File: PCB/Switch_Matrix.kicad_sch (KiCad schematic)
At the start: 28 parts, among them SW3 RotaryEncoder_Switch, SW4 RotaryEncoder_Switch

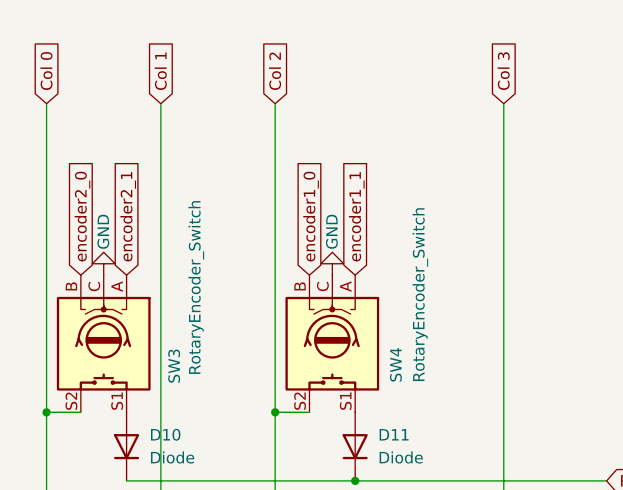
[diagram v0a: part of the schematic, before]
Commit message: Schema for V2 Did some cleanup and seperated the switch matrix to it's own file fixes #1
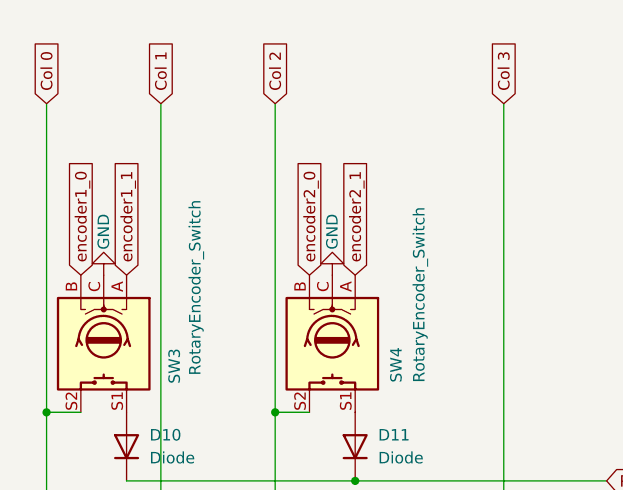
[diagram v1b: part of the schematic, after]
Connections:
- net encoder1_0: now also SW3.B; no longer SW4.B
- net encoder1_1: now also SW3.A; no longer SW4.A
- net encoder2_0: now also SW4.B; no longer SW3.B
- net encoder2_1: now also SW4.A; no longer SW3.A
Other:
- company: (none) -> KillrOfLife
- title: (none) -> Macro32
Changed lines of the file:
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@@
 	(generator_version "9.0")
 	(paper "A4")
+	(title_block
+		(title "Macro32")
+		(date "2025-11-08")
+		(rev "v2")
+		(company "KillrOfLife")
+	)
 	(junction
 		(at 72.39 128.27)
@@
 		)
 	)
+	(global_label "Col 1"
+		(shape input)
+		(at 54.61 38.1 90)
+		(fields_autoplaced yes)
+		(effects
+			(font
+				(size 1.27 1.27)
+			)
+			(justify left)
+		)
+		(property "Intersheetrefs" "${INTERSHEET_REFS}"
+			(at 54.61 29.8535 90)
+			(effects
+				(font
+					(size 1.27 1.27)
+				)
+				(justify left)
+				(hide yes)
+			)
+		)
+	)
+	(global_label "Col 0"
+		(shape input)
+		(at 41.91 38.1 90)
+		(fields_autoplaced yes)
+		(effects
+			(font
+				(size 1.27 1.27)
+			)
+			(justify left)
+		)
+		(property "Intersheetrefs" "${INTERSHEET_REFS}"
+			(at 41.91 29.8535 90)
+			(effects
+				(font
+					(size 1.27 1.27)
+				)
+				(justify left)
+				(hide yes)
+			)
+		)
+	)
+	(global_label "Col 2"
+		(shape input)
+		(at 67.31 38.1 90)
+		(fields_autoplaced yes)
+		(effects
+			(font
+				(size 1.27 1.27)
+			)
+			(justify left)
+		)
+		(property "Intersheetrefs" "${INTERSHEET_REFS}"
+			(at 67.31 29.8535 90)
+			(effects
+				(font
+					(size 1.27 1.27)
+				)
+				(justify left)
+				(hide yes)
+			)
+		)
+	)
+	(global_label "Row 0"
+		(shape input)
+		(at 104.14 80.01 0)
+		(fields_autoplaced yes)
+		(effects
+			(font
+				(size 1.27 1.27)
+			)
+			(justify left)
+		)
+		(property "Intersheetrefs" "${INTERSHEET_REFS}"
+			(at 113.0518 80.01 0)
+			(effects
+				(font
+					(size 1.27 1.27)
+				)
+				(justify left)
+				(hide yes)
+			)
+		)
+	)
+	(global_label "encoder1_1"
+		(shape input)
+		(at 50.8 57.15 90)
+		(fields_autoplaced yes)
+		(effects
+			(font
+				(size 1.27 1.27)
+			)
+			(justify left)
+		)
+		(property "Intersheetrefs" "${INTERSHEET_REFS}"
+			(at 50.8 43.2792 90)
+			(effects
+				(font
+					(size 1.27 1.27)
+				)
+				(justify left)
+				(hide yes)
+			)
+		)
+	)
+	(global_label "Row 3"
+		(shape input)
+		(at 105.41 153.67 0)
+		(fields_autoplaced yes)
+		(effects
+			(font
+				(size 1.27 1.27)
+			)
+			(justify left)
+		)
+		(property "Intersheetrefs" "${INTERSHEET_REFS}"
+			(at 114.3218 153.67 0)
+			(effects
+				(font
+					(size 1.27 1.27)
+				)
+				(justify left)
+				(hide yes)
+			)
+		)
+	)
+	(global_label "encoder2_1"
+		(shape input)
+		(at 76.2 57.15 90)
+		(fields_autoplaced yes)
+		(effects
+			(font
+				(size 1.27 1.27)
+			)
+			(justify left)
+		)
+		(property "Intersheetrefs" "${INTERSHEET_REFS}"
+			(at 76.2 43.2792 90)
+			(effects
+				(font
+					(size 1.27 1.27)
+				)
+				(justify left)
+				(hide yes)
+			)
+		)
+	)
 	(global_label "encoder2_0"
 		(shape input)
+		(at 71.12 57.15 90)
+		(fields_autoplaced yes)
+		(effects
+			(font
+				(size 1.27 1.27)
+			)
+			(justify left)
+		)
+		(property "Intersheetrefs" "${INTERSHEET_REFS}"
+			(at 71.12 43.2792 90)
+			(effects
+				(font
+					(size 1.27 1.27)
+				)
+				(justify left)
+				(hide yes)
+			)
+		)
+	)
+	(global_label "encoder1_0"
+		(shape input)
 		(at 45.72 57.15 90)
 		(fields_autoplaced yes)
@@
 			(effects
 				(font
-					(size 1.27 1.27)
-				)
-				(justify left)
-				(hide yes)
-			)
-		)
-	)
-	(global_label "encoder1_1"
-		(shape input)
-		(at 76.2 57.15 90)
-		(fields_autoplaced yes)
-		(effects
-			(font
-				(size 1.27 1.27)
-			)
-			(justify left)
-		)
-		(property "Intersheetrefs" "${INTERSHEET_REFS}"
-			(at 76.2 43.2792 90)
-			(effects
-				(font
-					(size 1.27 1.27)
-				)
-				(justify left)
-				(hide yes)
-			)
-		)
-	)
-	(global_label "Col 1"
-		(shape input)
-		(at 54.61 38.1 90)
-		(fields_autoplaced yes)
-		(effects
-			(font
-				(size 1.27 1.27)
-			)
-			(justify left)
-		)
-		(property "Intersheetrefs" "${INTERSHEET_REFS}"
-			(at 54.61 29.8535 90)
-			(effects
-				(font
-					(size 1.27 1.27)
-				)
-				(justify left)
-				(hide yes)
-			)
-		)
-	)
-	(global_label "Col 0"
-		(shape input)
-		(at 41.91 38.1 90)
-		(fields_autoplaced yes)
-		(effects
-			(font
-				(size 1.27 1.27)
-			)
-			(justify left)
-		)
-		(property "Intersheetrefs" "${INTERSHEET_REFS}"
-			(at 41.91 29.8535 90)
-			(effects
-				(font
-					(size 1.27 1.27)
-				)
-				(justify left)
-				(hide yes)
-			)
-		)
-	)
-	(global_label "Col 2"
-		(shape input)
-		(at 67.31 38.1 90)
-		(fields_autoplaced yes)
-		(effects
-			(font
-				(size 1.27 1.27)
-			)
-			(justify left)
-		)
-		(property "Intersheetrefs" "${INTERSHEET_REFS}"
-			(at 67.31 29.8535 90)
-			(effects
-				(font
-					(size 1.27 1.27)
-				)
-				(justify left)
-				(hide yes)
-			)
-		)
-	)
-	(global_label "encoder2_1"
-		(shape input)
-		(at 50.8 57.15 90)
-		(fields_autoplaced yes)
-		(effects
-			(font
-				(size 1.27 1.27)
-			)
-			(justify left)
-		)
-		(property "Intersheetrefs" "${INTERSHEET_REFS}"
-			(at 50.8 43.2792 90)
-			(effects
-				(font
-					(size 1.27 1.27)
-				)
-				(justify left)
-				(hide yes)
-			)
-		)
-	)
-	(global_label "encoder1_0"
-		(shape input)
-		(at 71.12 57.15 90)
-		(fields_autoplaced yes)
-		(effects
-			(font
-				(size 1.27 1.27)
-			)
-			(justify left)
-		)
-		(property "Intersheetrefs" "${INTERSHEET_REFS}"
-			(at 71.12 43.2792 90)
-			(effects
-				(font
-					(size 1.27 1.27)
-				)
-				(justify left)
-				(hide yes)
-			)
-		)
-	)
-	(global_label "Row 0"
-		(shape input)
-		(at 104.14 80.01 0)
-		(fields_autoplaced yes)
-		(effects
-			(font
-				(size 1.27 1.27)
-			)
-			(justify left)
-		)
-		(property "Intersheetrefs" "${INTERSHEET_REFS}"
-			(at 113.0518 80.01 0)
-			(effects
-				(font
-					(size 1.27 1.27)
-				)
-				(justify left)
-				(hide yes)
-			)
-		)
-	)
-	(global_label "Row 3"
-		(shape input)
-		(at 105.41 153.67 0)
-		(fields_autoplaced yes)
-		(effects
-			(font
-				(size 1.27 1.27)
-			)
-			(justify left)
-		)
-		(property "Intersheetrefs" "${INTERSHEET_REFS}"
-			(at 114.3218 153.67 0)
-			(effects
-				(font

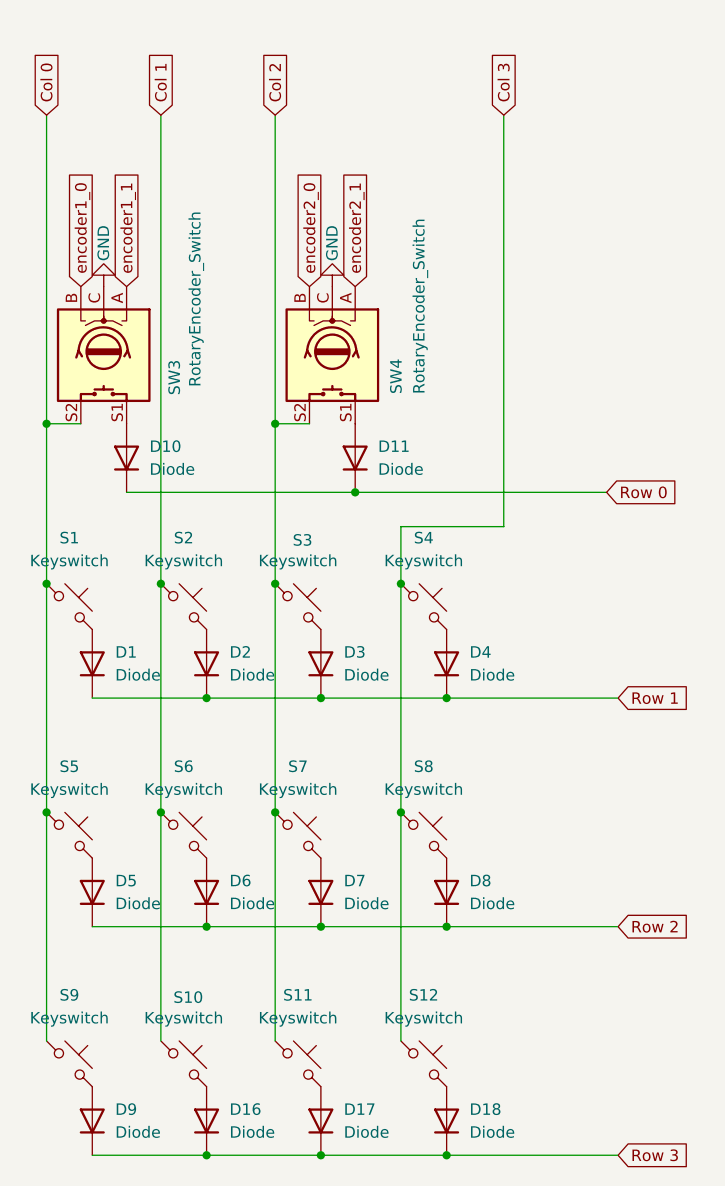
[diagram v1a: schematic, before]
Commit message: Adjust PCB layout and added magnetic connector for modularity
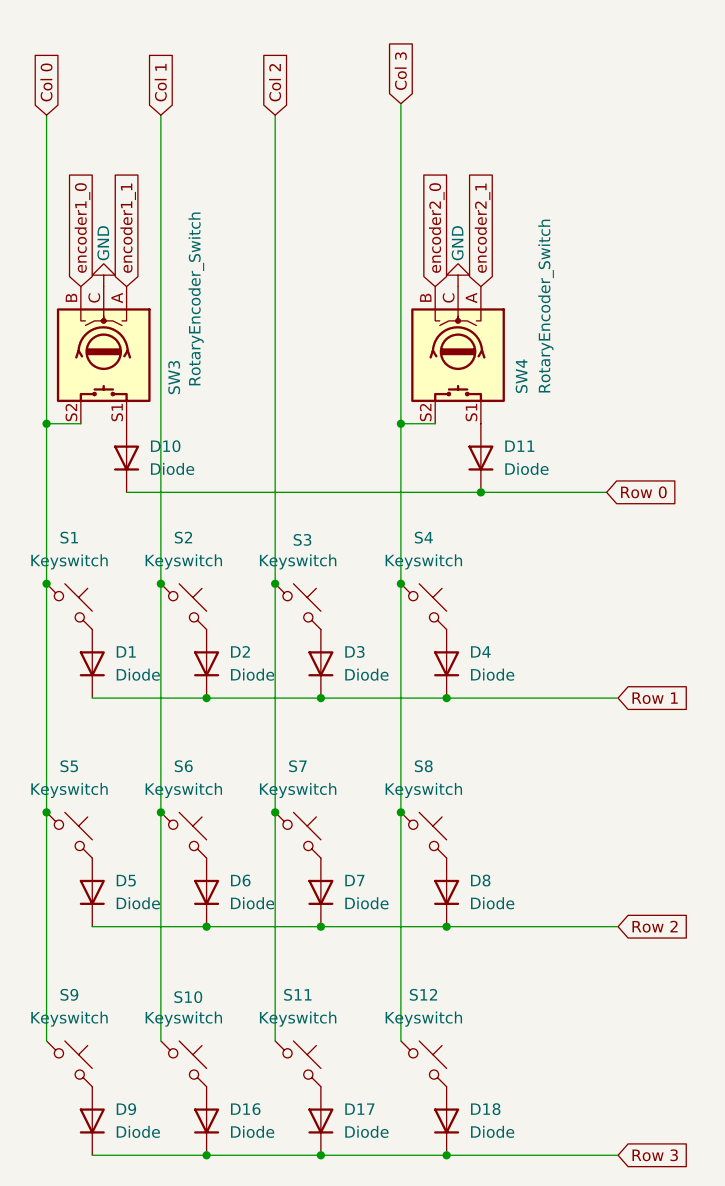
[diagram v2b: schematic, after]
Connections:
- net Col 2: no longer SW4.S2
- net Col 3: now also SW4.S2
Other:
- moved on the sheet: D11, SW4
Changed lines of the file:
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@@
-	)
-	(junction
-		(at 67.31 72.39)
-		(diameter 0)
-		(color 0 0 0 0)
-	)
-	(junction
-		(at 76.2 80.01)
-		(diameter 0)
-		(color 0 0 0 0)
 	)
 	(junction
@@
 	)
 	(junction
+		(at 81.28 72.39)
+		(diameter 0)
+		(color 0 0 0 0)
+	)
+	(junction
 		(at 86.36 102.87)
 		(diameter 0)
@@
 	)
 	(junction
+		(at 90.17 80.01)
+		(diameter 0)
+		(color 0 0 0 0)
+	)
+	(junction
 		(at 54.61 115.57)
 		(diameter 0)
@@
 	(wire
 		(pts
+			(xy 81.28 72.39) (xy 81.28 90.17)
+		)
+		(stroke
+			(width 0)
+			(type default)
+		)
+	)
+	(wire
+		(pts
 			(xy 86.36 128.27) (xy 105.41 128.27)
 		)
@@
 	(wire
 		(pts
+			(xy 90.17 80.01) (xy 104.14 80.01)
+		)
+		(stroke
+			(width 0)
+			(type default)
+		)
+	)
+	(wire
+		(pts
 			(xy 81.28 90.17) (xy 81.28 115.57)
 		)
@@
 	(wire
 		(pts
-			(xy 76.2 80.01) (xy 104.14 80.01)
-		)
-		(stroke
-			(width 0)
-			(type default)
-		)
-	)
-	(wire
-		(pts
-			(xy 50.8 80.01) (xy 76.2 80.01)
-		)
-		(stroke
-			(width 0)
-			(type default)
-		)
-	)
-	(wire
-		(pts
-			(xy 67.31 72.39) (xy 67.31 90.17)
+			(xy 50.8 80.01) (xy 90.17 80.01)
+		)
+		(stroke
+			(width 0)
+			(type default)
+		)
+	)
+	(wire
+		(pts
+			(xy 67.31 38.1) (xy 67.31 90.17)
+		)
+		(stroke
+			(width 0)
+			(type default)
+		)
+	)
+	(wire
+		(pts
+			(xy 81.28 72.39) (xy 85.09 72.39)
 		)
 		(stroke
@@
 	(wire
 		(pts
-			(xy 92.71 38.1) (xy 92.71 83.82)
-		)
-		(stroke
-			(width 0)
-			(type default)
-		)
-	)
-	(wire
-		(pts
 			(xy 41.91 38.1) (xy 41.91 72.39)
 		)
@@
 	(wire
 		(pts
-			(xy 67.31 72.39) (xy 71.12 72.39)
-		)
-		(stroke
-			(width 0)
-			(type default)
-		)
-	)
-	(wire
-		(pts
 			(xy 41.91 72.39) (xy 41.91 90.17)
 		)
@@
 	(wire
 		(pts
-			(xy 81.28 83.82) (xy 92.71 83.82)
-		)
-		(stroke
-			(width 0)
-			(type default)
-		)
-	)
-	(wire
-		(pts
 			(xy 54.61 90.17) (xy 54.61 115.57)
 		)
@@
 	(wire
 		(pts
-			(xy 67.31 38.1) (xy 67.31 72.39)
-		)
-		(stroke
-			(width 0)
-			(type default)
-		)
-	)
-	(wire
-		(pts
-			(xy 81.28 83.82) (xy 81.28 90.17)
+			(xy 81.28 36.83) (xy 81.28 72.39)
 		)
 		(stroke
@@
 		)
 	)
+	(global_label "encoder2_0"
+		(shape input)
+		(at 85.09 57.15 90)
+		(fields_autoplaced yes)
+		(effects
+			(font
+				(size 1.27 1.27)
+			)
+			(justify left)
+		)
+		(property "Intersheetrefs" "${INTERSHEET_REFS}"
+			(at 85.09 43.2792 90)
+			(effects
+				(font
+					(size 1.27 1.27)
+				)
+				(justify left)
+				(hide yes)
+			)
+		)
+	)
 	(global_label "Col 2"
 		(shape input)
@@
 		)
 	)
+	(global_label "encoder2_1"
+		(shape input)
+		(at 90.17 57.15 90)
+		(fields_autoplaced yes)
+		(effects
+			(font
+				(size 1.27 1.27)
+			)
+			(justify left)
+		)
+		(property "Intersheetrefs" "${INTERSHEET_REFS}"
+			(at 90.17 43.2792 90)
+			(effects
+				(font
+					(size 1.27 1.27)
+				)
+				(justify left)
+				(hide yes)
+			)
+		)
+	)
 	(global_label "Row 0"
 		(shape input)
@@
 		)
 	)
-	(global_label "encoder2_1"
+	(global_label "encoder1_0"
 		(shape input)
-		(at 76.2 57.15 90)
+		(at 45.72 57.15 90)
 		(fields_autoplaced yes)
 		(effects
@@
 		)
 		(property "Intersheetrefs" "${INTERSHEET_REFS}"
-			(at 76.2 43.2792 90)
+			(at 45.72 43.2792 90)
 			(effects
 				(font
@@
 		)
 	)
-	(global_label "encoder2_0"
+	(global_label "Col 3"
 		(shape input)
-		(at 71.12 57.15 90)
+		(at 81.28 36.83 90)
 		(fields_autoplaced yes)
 		(effects
@@
 		)
 		(property "Intersheetrefs" "${INTERSHEET_REFS}"
-			(at 71.12 43.2792 90)
-			(effects
-				(font
-					(size 1.27 1.27)
-				)
-				(justify left)
-				(hide yes)
-			)
-		)
-	)
-	(global_label "encoder1_0"
-		(shape input)
-		(at 45.72 57.15 90)
-		(fields_autoplaced yes)
-		(effects
-			(font
-				(size 1.27 1.27)
-			)
-			(justify left)
-		)
-		(property "Intersheetrefs" "${INTERSHEET_REFS}"
-			(at 45.72 43.2792 90)
-			(effects
-				(font
-					(size 1.27 1.27)
-				)
-				(justify left)
-				(hide yes)
-			)
-		)
-	)
-	(global_label "Col 3"
-		(shape input)
-		(at 92.71 38.1 90)
-		(fields_autoplaced yes)
-		(effects
-			(font
-				(size 1.27 1.27)
-			)
-			(justify left)
-		)
-		(property "Intersheetrefs" "${INTERSHEET_REFS}"
-			(at 92.71 29.8535 90)
+			(at 81.28 28.5835 90)
 			(effects
 				(font
@@
 	(symbol
 		(lib_id "power:GND")
-		(at 73.66 57.15 180)
+		(at 87.63 57.15 180)
 		(unit 1)
 		(exclude_from_sim no)
@@
 		(dnp no)
 		(property "Reference" "#PWR018"
-			(at 73.66 50.8 0)
+			(at 87.63 50.8 0)
 			(effects
 				(font
@@
 		)
 		(property "Value" "GND"
-			(at 73.66 52.324 90)
+			(at 87.63 52.324 90)
 			(effects
 				(font
@@
 		)
 		(property "Footprint" ""
-			(at 73.66 57.15 0)
+			(at 87.63 57.15 0)
 			(effects
 				(font
@@
 		)
 		(property "Datasheet" ""
-			(at 73.66 57.15 0)
+			(at 87.63 57.15 0)
 			(effects
 				(font
@@
 		)
 		(property "Description" "Power symbol creates a global label with name \"GND\" , ground"
-			(at 73.66 57.15 0)
+			(at 87.63 57.15 0)
 			(effects
 				(font
@@
 	(symbol
 		(lib_id "ScottoKeebs:Placeholder_Diode")
-		(at 76.2 76.2 90)
+		(at 90.17 76.2 90)
 		(unit 1)
 		(exclude_from_sim no)
@@
 		(fields_autoplaced yes)
 		(property "Reference" "D11"
-			(at 78.74 74.9299 90)
+			(at 92.71 74.9299 90)
 			(effects
 				(font
@@
 		)
 		(property "Value" "Diode"
-			(at 78.74 77.4699 90)
+			(at 92.71 77.4699 90)
 			(effects
 				(font
@@
 		)
 		(property "Footprint" "ScottoKeebs_Components:Diode_SOD-123"
-			(at 76.2 76.2 0)
+			(at 90.17 76.2 0)
 			(effects
 				(font
@@
 		)
 		(property "Datasheet" ""
-			(at 76.2 76.2 0)
+			(at 90.17 76.2 0)
 			(effects
 				(font
@@
 		)
 		(property "Description" "1N4148 (DO-35) or 1N4148W (SOD-123)"
-			(at 76.2 76.2 0)
+			(at 90.17 76.2 0)
 			(effects
 				(font
@@
 		)
 		(property "Sim.Device" "D"
-			(at 76.2 76.2 0)
+			(at 90.17 76.2 0)
 			(effects
 				(font
@@
 		)
 		(property "Sim.Pins" "1=K 2=A"
-			(at 76.2 76.2 0)
+			(at 90.17 76.2 0)
 			(effects
 				(font
@@
 	(symbol
 		(lib_id "Device:RotaryEncoder_Switch")
-		(at 73.66 64.77 270)
+		(at 87.63 64.77 270)
 		(unit 1)
 		(exclude_from_sim no)
@@
 		(dnp no)
 		(property "Reference" "SW4"
-			(at 80.772 69.088 0)
+			(at 94.742 69.088 0)
 			(effects
 				(font
@@
 		)
 		(property "Value" "RotaryEncoder_Switch"
-			(at 83.312 69.088 0)
+			(at 97.282 69.088 0)
 			(effects
 				(font
@@
 		)
 		(property "Footprint" "kbd:keyswitch_cherrymx_hotswap_1u_rotary_encoder_ec12"
-			(at 77.724 60.96 0)
+			(at 91.694 60.96 0)
 			(effects
 				(font
@@
 		)
 		(property "Datasheet" "~"
-			(at 80.264 64.77 0)
+			(at 94.234 64.77 0)
 			(effects
 				(font
@@
 		)
 		(property "Description" "Rotary encoder, dual channel, incremental quadrate outputs, with switch"
-			(at 73.66 64.77 0)
-			(effects
-				(font
+			(at 87.63 64.77 0)
+			(effects
+				(font
